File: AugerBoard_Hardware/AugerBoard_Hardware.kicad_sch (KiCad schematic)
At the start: 48 parts, among them J1 RJ45_LED_Shielded, SW1 SW_SPDT, SW2 SW_Push, SW3 SW_Push, SW4 SW_Push, SW5 SW_Push, U1 Teensy4.1_DEV-16771, U2 OKI-78SR-5_1.5-W36H-C

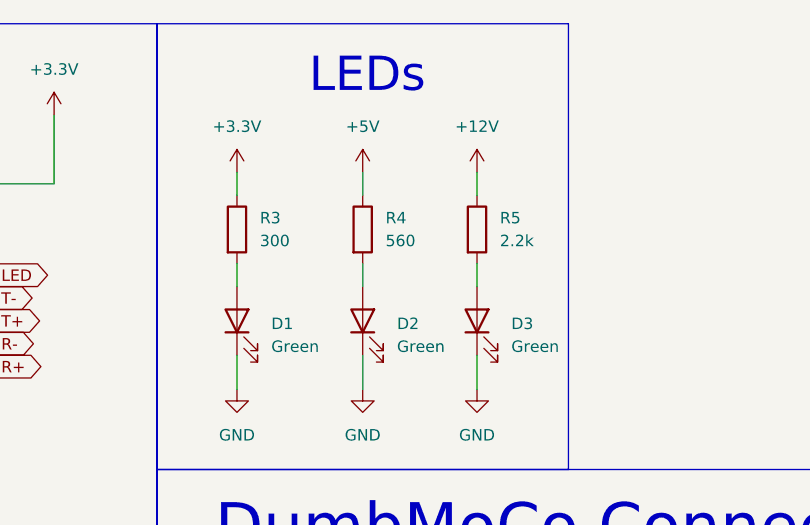
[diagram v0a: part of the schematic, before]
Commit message: Fixed LED resistor value
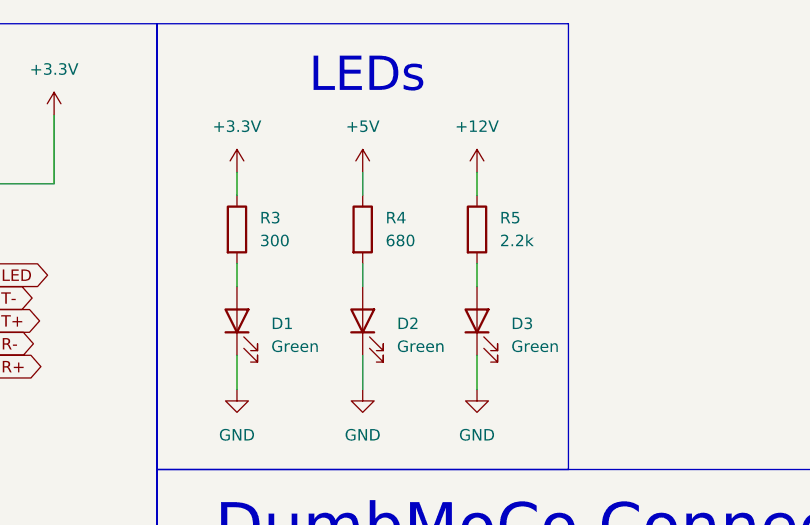
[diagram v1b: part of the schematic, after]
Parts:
- R4: value 560 -> 680
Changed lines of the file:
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@@
 			)
 		)
-		(property "Value" "560"
+		(property "Value" "680"
 			(at 313.69 38.0999 0)
 			(effects

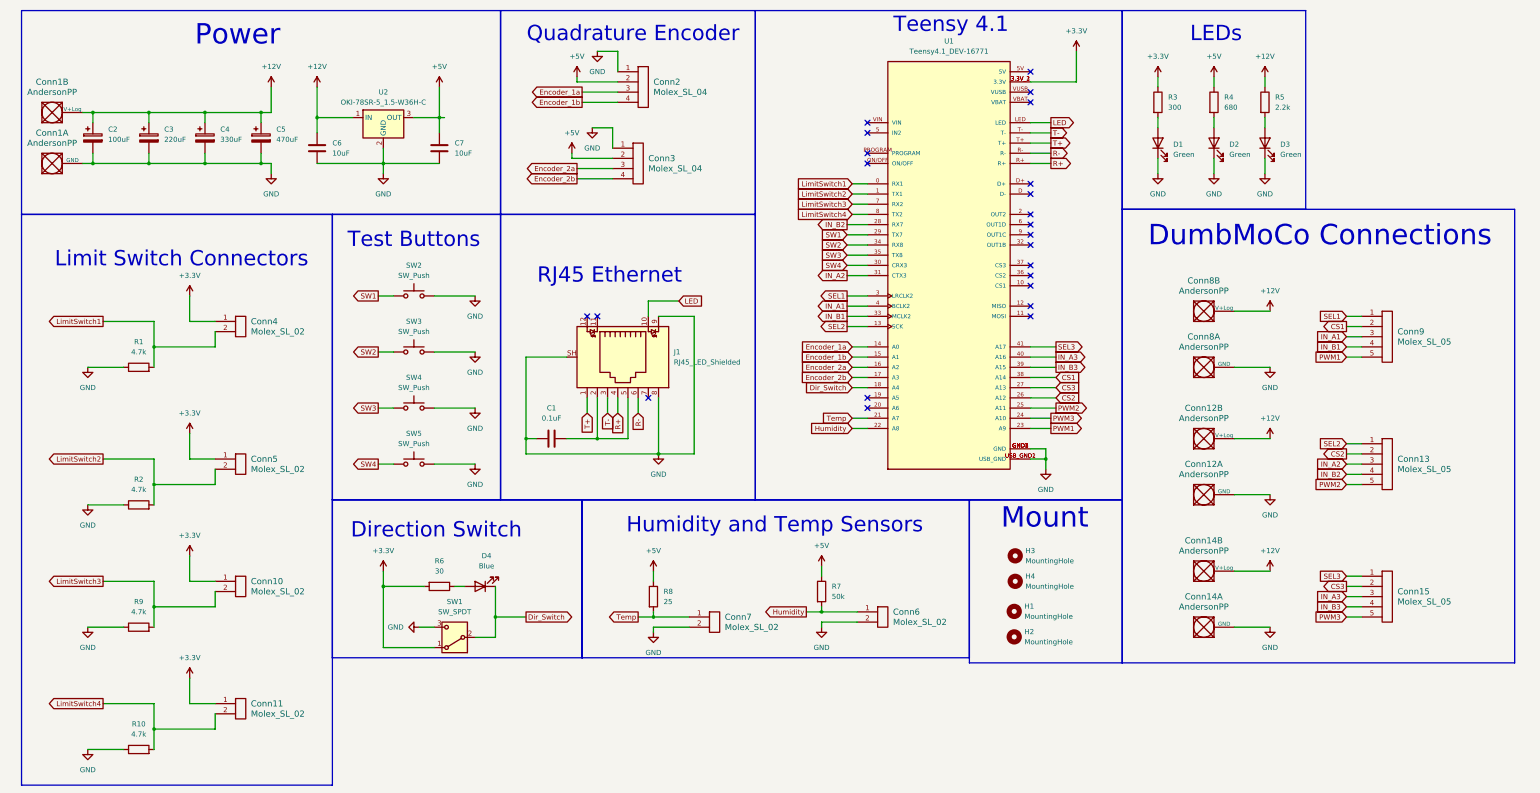
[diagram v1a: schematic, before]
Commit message: some schematic review changes
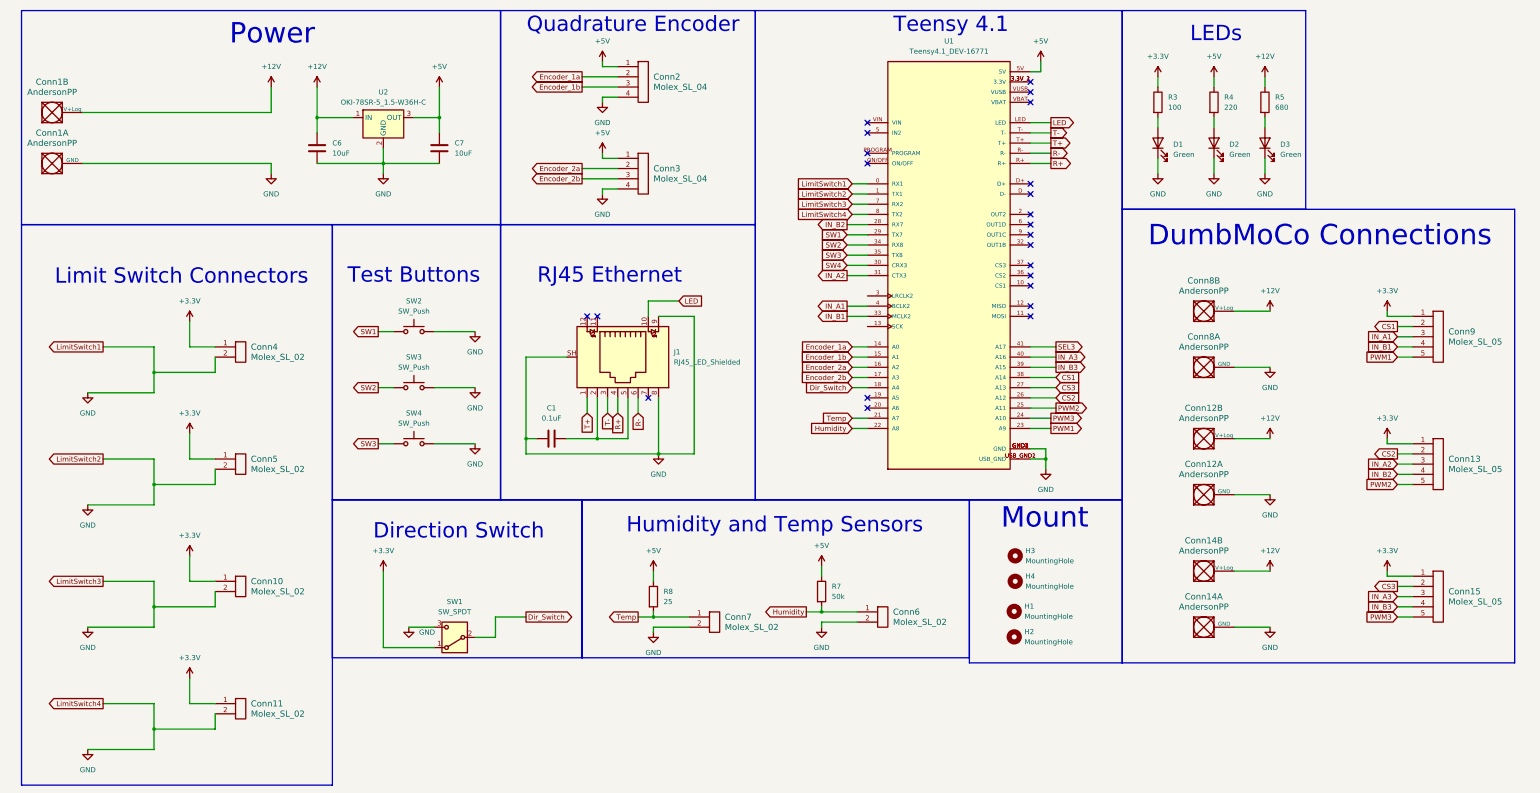
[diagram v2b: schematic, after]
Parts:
- removed C2: 100uF, symbol Device:C_Polarized
- removed C3: 220uF, symbol Device:C_Polarized
- removed C4: 330uF, symbol Device:C_Polarized
- removed C5: 470uF, symbol Device:C_Polarized
- removed D4: Blue, symbol Device:LED
- removed R1, R10, R2, R9: 4.7k, symbol Device:R
- removed R6: 30, symbol Device:R
- removed SW5: SW_Push, symbol Switch:SW_Push
- R3: value 300 -> 100
- R4: value 680 -> 220
- R5: value 2.2k -> 680
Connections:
- net LimitSwitch1 is gone; now on net GND: Conn4.2, U1.0 (RX1)
- net LimitSwitch2 is gone; now on net GND: Conn5.2, U1.1 (TX1)
- net LimitSwitch3 is gone; now on net GND: Conn10.2, U1.7 (RX2)
- net LimitSwitch4 is gone; now on net GND: Conn11.2, U1.8 (TX2)
- net +3.3V: now also Conn13.1, Conn15.1, Conn9.1; no longer U1.3.3V_1 (3.3V), U1.3.3V_2 (3.3V), U1.3.3V_3 (3.3V)
- net +5V: now also Conn2.1, Conn3.1, U1.5V; no longer Conn2.2, Conn3.2
- net Encoder_1a: now also Conn2.2; no longer Conn2.3
- net Encoder_1b: now also Conn2.3; no longer Conn2.4
- net Encoder_2a: now also Conn3.2; no longer Conn3.3
- net Encoder_2b: now also Conn3.3; no longer Conn3.4
- net GND: now also Conn2.4, Conn3.4; no longer Conn2.1, Conn3.1
- net SEL3: no longer Conn15.1
- net SEL1: no longer names the net of U1.3 (LRCLK2)
- net SEL1: no longer Conn9.1
- net SEL2: no longer names the net of U1.13 (SCK)
- net SEL2: no longer Conn13.1
- new net: U1.3.3V_1 (3.3V), U1.3.3V_2 (3.3V), U1.3.3V_3 (3.3V)
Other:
- moved on the sheet: Conn13, Conn15, Conn2, Conn3, Conn4, Conn9, SW2, SW3, SW4

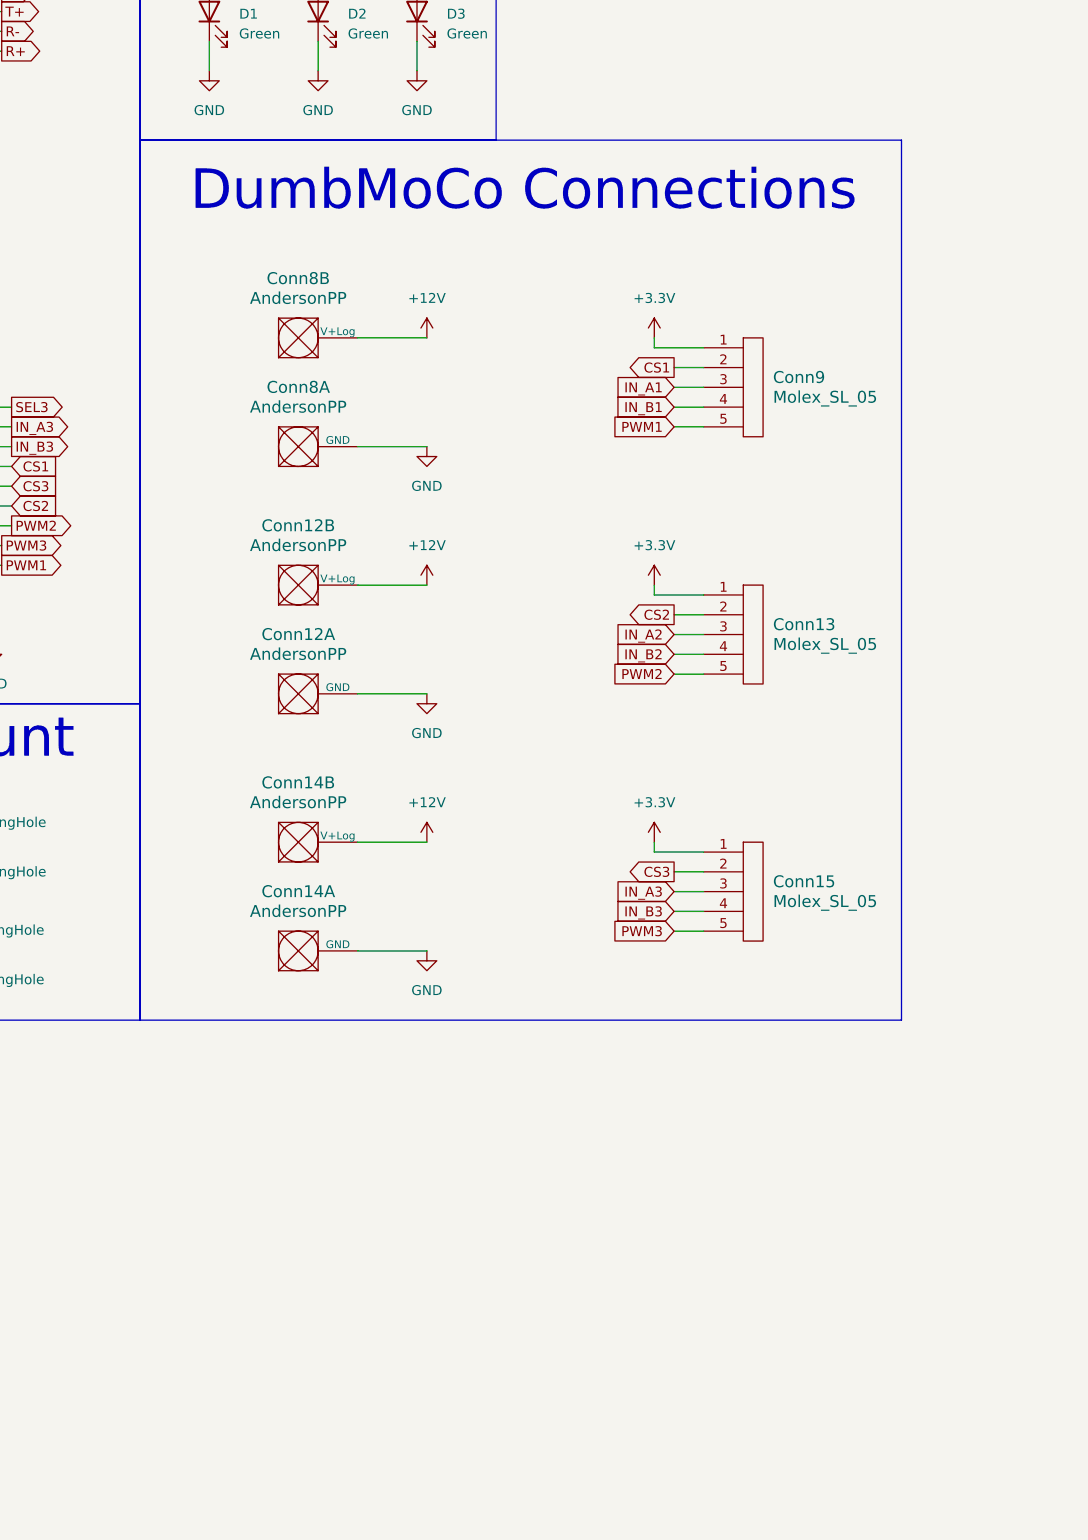
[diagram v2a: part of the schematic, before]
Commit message: Added PWM LED
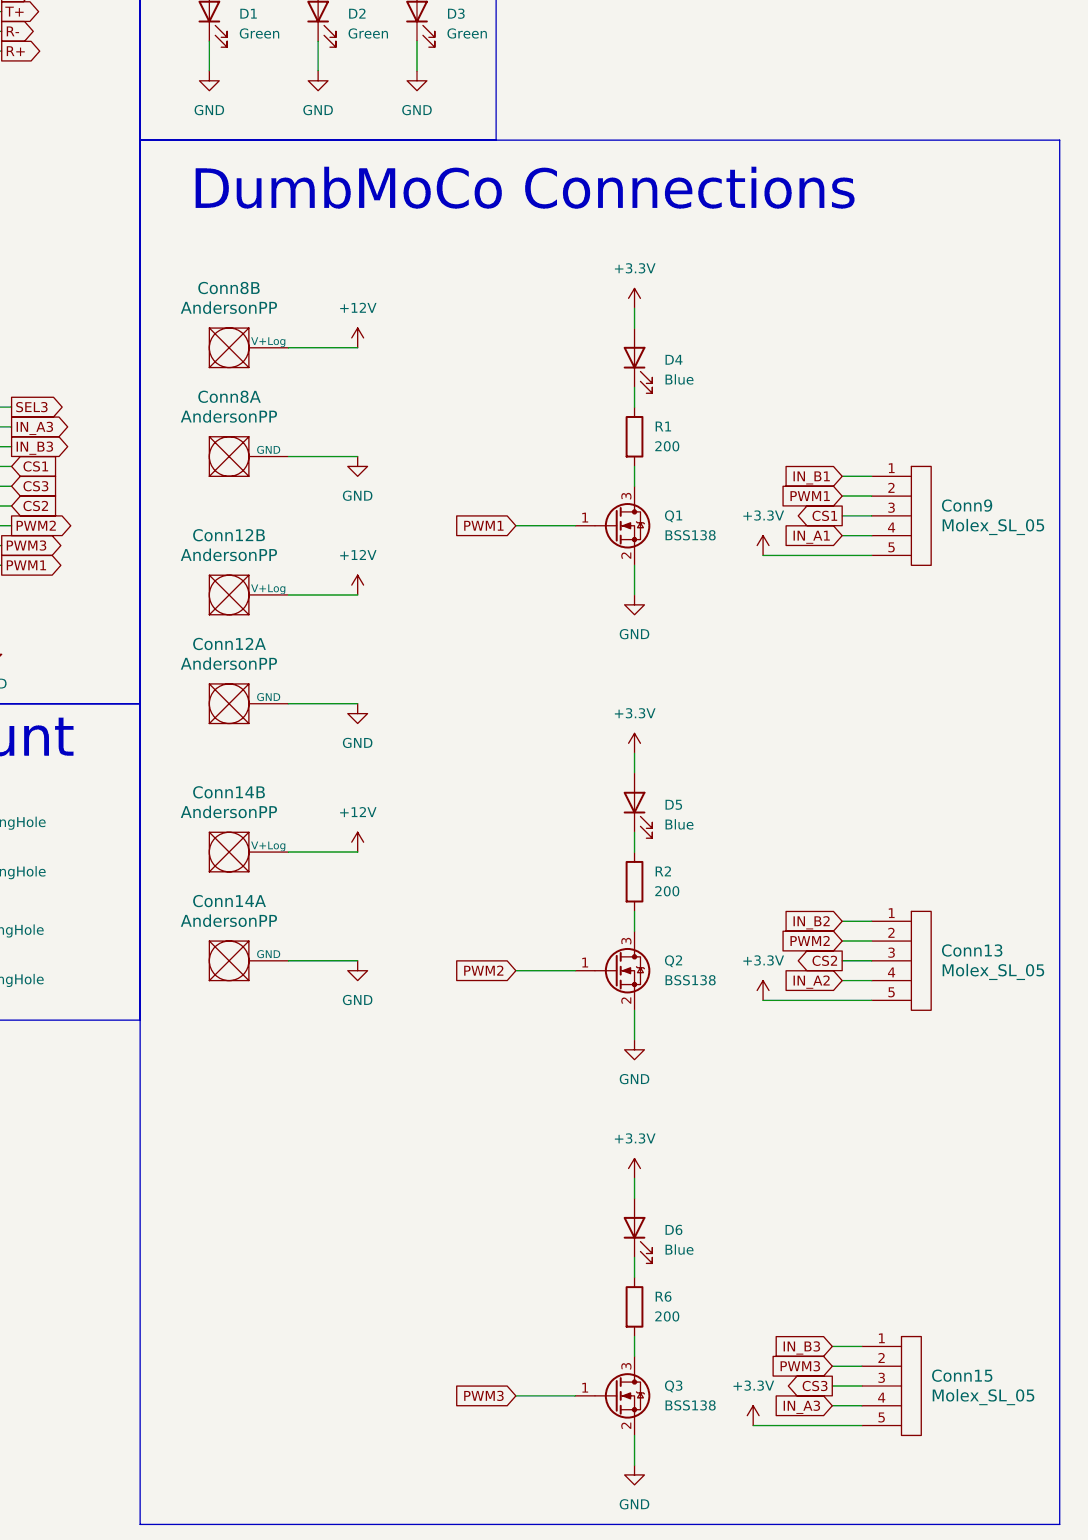
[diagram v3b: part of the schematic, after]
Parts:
- added D4, D5, D6: Blue, symbol Device:LED
- added Q1, Q2, Q3: BSS138, Package_TO_SOT_SMD:SOT-23, symbol Transistor_FET:BSS138
- added R1, R2, R6: 200, symbol Device:R
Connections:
- net +3.3V: now also Conn13.5, Conn15.5, Conn9.5, D4.2 (A), D5.2 (A), D6.2 (A); no longer Conn13.1, Conn15.1, Conn9.1
- net CS1: now also Conn9.3; no longer Conn9.2
- net CS2: now also Conn13.3; no longer Conn13.2
- net CS3: now also Conn15.3; no longer Conn15.2
- net GND: now also Q1.2 (S), Q2.2 (S), Q3.2 (S)
- net IN_A1: now also Conn9.4; no longer Conn9.3
- net IN_A2: now also Conn13.4; no longer Conn13.3
- net IN_A3: now also Conn15.4; no longer Conn15.3
- net IN_B1: now also Conn9.1; no longer Conn9.4
- net IN_B2: now also Conn13.1; no longer Conn13.4
- net IN_B3: now also Conn15.1; no longer Conn15.4
- net PWM1: now also Conn9.2, Q1.1 (G); no longer Conn9.5
- net PWM2: now also Conn13.2, Q2.1 (G); no longer Conn13.5
- net PWM3: now also Conn15.2, Q3.1 (G); no longer Conn15.5
- new net: Q3.3 (D), R6.2
- new net: D4.1 (K), R1.1
- new net: D6.1 (K), R6.1
- new net: Q1.3 (D), R1.2
- new net: D5.1 (K), R2.1
- new net: Q2.3 (D), R2.2
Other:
- moved on the sheet: Conn12A, Conn12B, Conn14A, Conn14B, Conn8A, Conn8B, Conn9

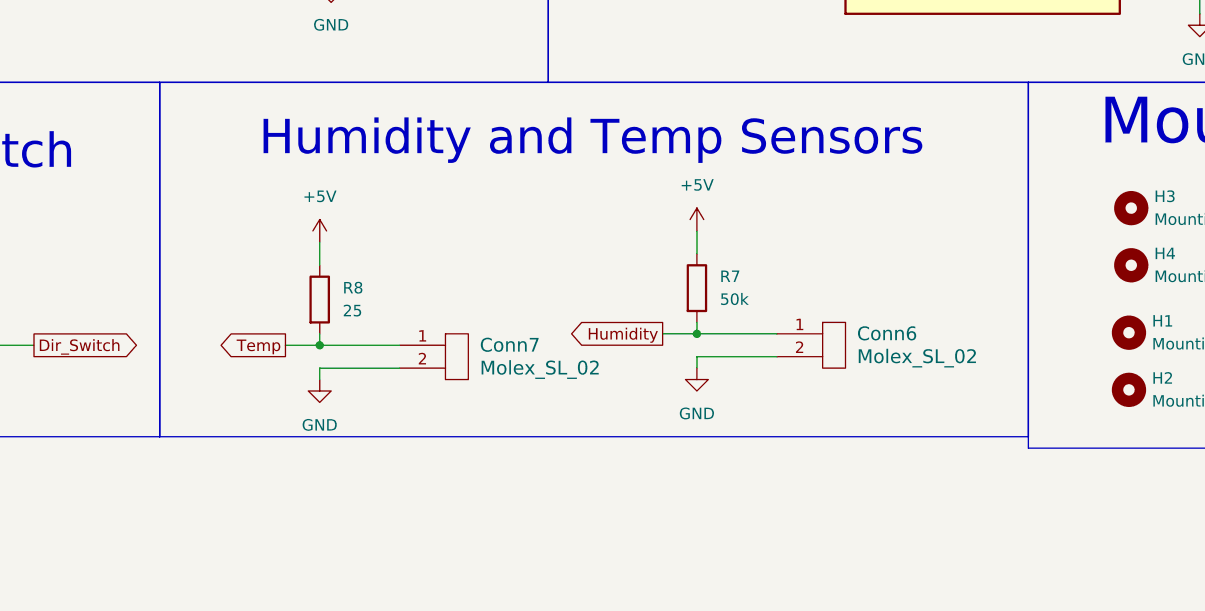
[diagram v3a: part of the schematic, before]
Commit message: Updated sensor circuits and updated BOM
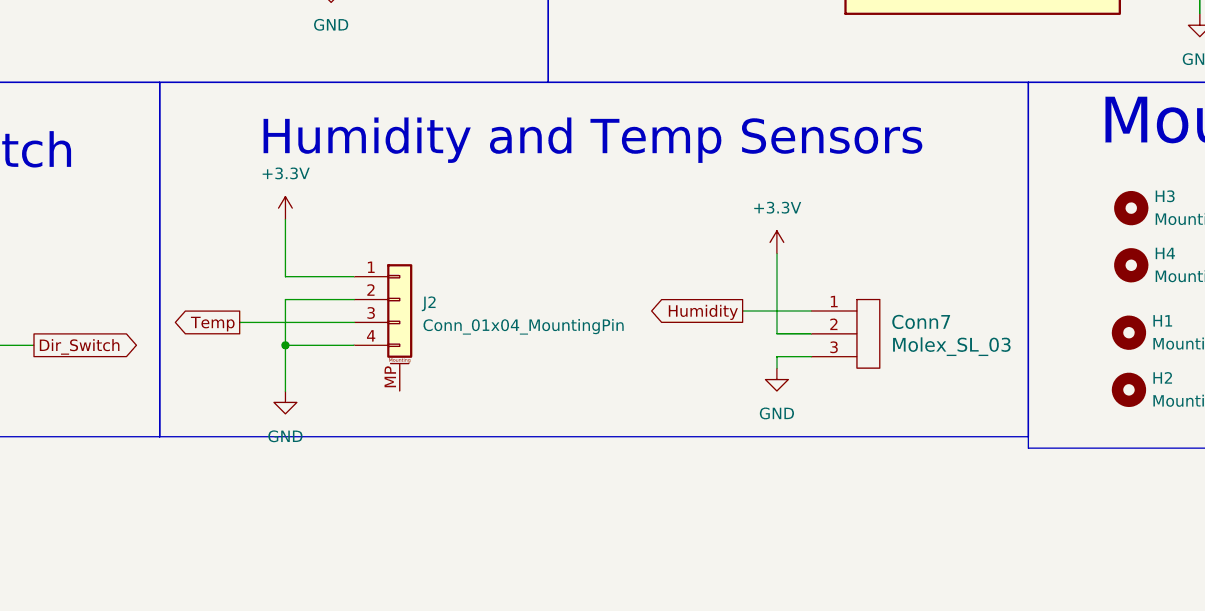
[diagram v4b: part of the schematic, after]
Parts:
- removed Conn6, Conn7: Molex_SL_02, symbol MRDT_Connectors:Molex_SL_02
- removed R7: 50k, symbol Device:R
- removed R8: 25, symbol Device:R
- added Conn7: Molex_SL_03, symbol MRDT_Connectors:Molex_SL_03
- added J2: Conn_01x04_MountingPin, symbol Connector_Generic_MountingPin:Conn_01x04_MountingPin
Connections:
- net +3.3V: now also Conn7.2, J2.1 (Pin_1)
- net GND: now also Conn7.3, J2.2 (Pin_2), J2.4 (Pin_4)
- net Humidity: now also Conn7.1
- net Temp: now also J2.3 (Pin_3)
